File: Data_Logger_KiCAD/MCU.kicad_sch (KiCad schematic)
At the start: 39 parts, among them J1 USB_C_Receptacle_USB2.0_16P, J2 Screw_Terminal_01x02, Q1 Q_NMOS_GSD, SW1 SW_Push, SW2 SW_Push, U2 ESP32-S3, Y2 Crystal, Y3 Crystal_GND24

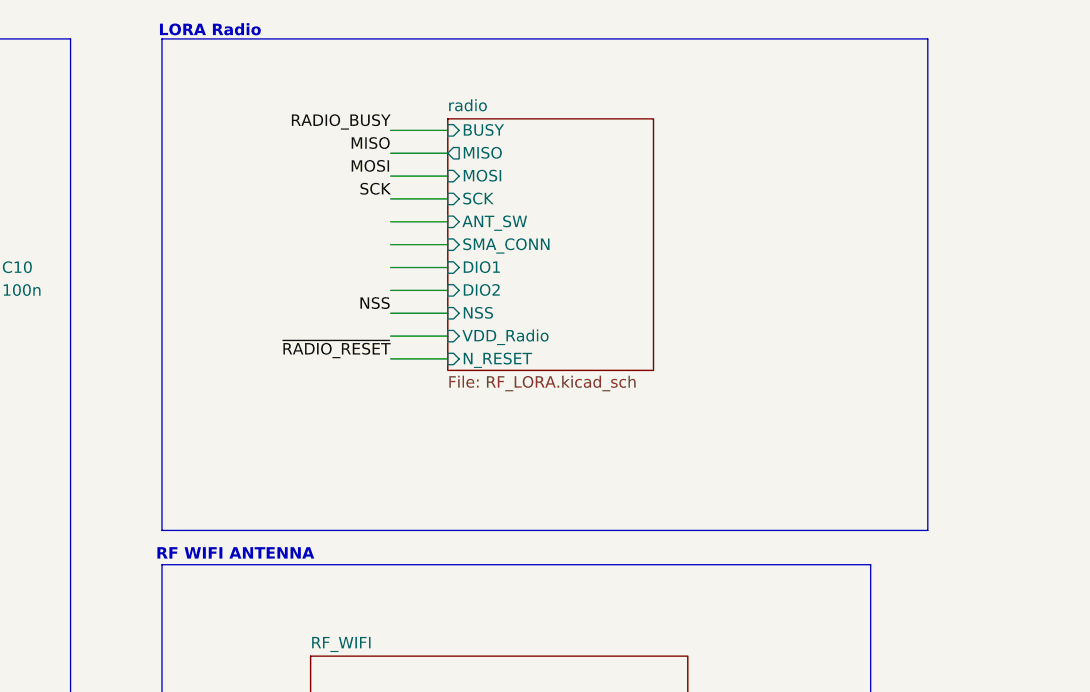
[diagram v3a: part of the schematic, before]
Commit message: update sheet pins
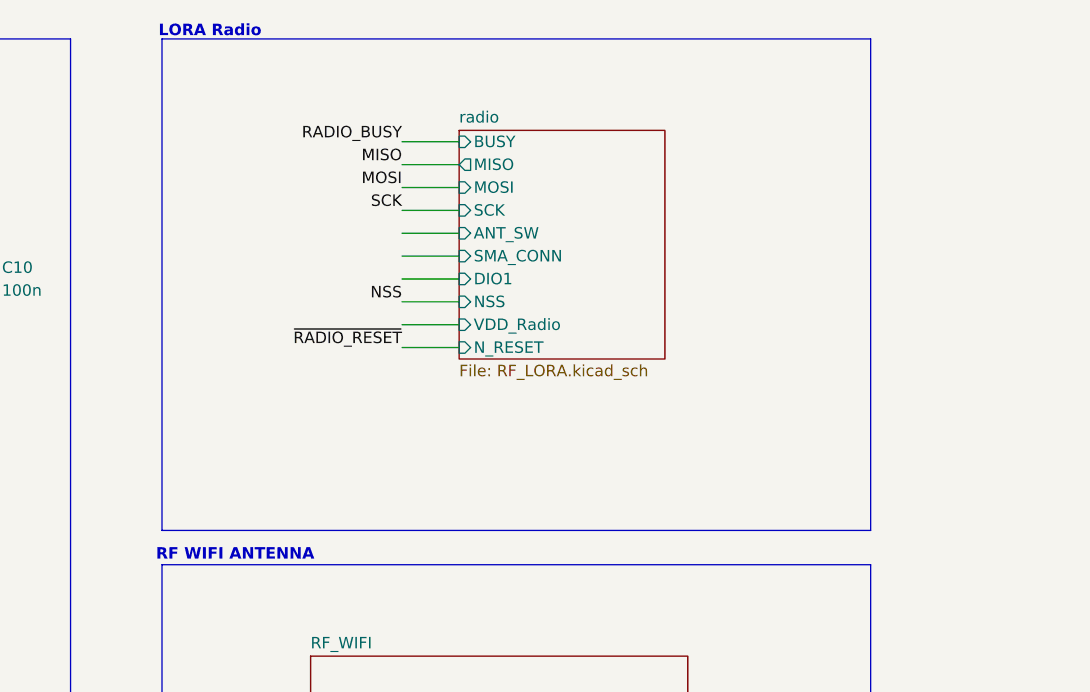
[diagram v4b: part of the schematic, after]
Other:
- sheet radio ports: added none; removed DIO2
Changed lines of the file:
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@@
 	(rectangle
 		(start 242.57 53.34)
-		(end 327.66 107.95)
+		(end 321.31 107.95)
 		(stroke
 			(width 0)
@@
 	(wire
 		(pts
-			(xy 267.97 68.58) (xy 274.32 68.58)
+			(xy 269.24 69.85) (xy 275.59 69.85)
 		)
 		(stroke
@@
 	(wire
 		(pts
+			(xy 269.24 85.09) (xy 275.59 85.09)
+		)
+		(stroke
+			(width 0)
+			(type default)
+		)
+	)
+	(wire
+		(pts
 			(xy 66.04 72.39) (xy 68.58 72.39)
 		)
@@
 	(wire
 		(pts
+			(xy 269.24 87.63) (xy 275.59 87.63)
+		)
+		(stroke
+			(width 0)
+			(type default)
+		)
+	)
+	(wire
+		(pts
 			(xy 132.08 95.25) (xy 139.7 95.25)
 		)
@@
 	(wire
 		(pts
-			(xy 267.97 71.12) (xy 274.32 71.12)
+			(xy 269.24 72.39) (xy 275.59 72.39)
 		)
 		(stroke
@@
 	(wire
 		(pts
-			(xy 33.02 306.07) (xy 40.64 306.07)
+			(xy 269.24 82.55) (xy 275.59 82.55)
 		)
 		(stroke
@@
 	(wire
 		(pts
-			(xy 63.5 306.07) (xy 63.5 307.34)
+			(xy 33.02 306.07) (xy 40.64 306.07)
 		)
 		(stroke
@@
 	(wire
 		(pts
-			(xy 185.42 151.13) (xy 193.04 151.13)
+			(xy 63.5 306.07) (xy 63.5 307.34)
 		)
 		(stroke
@@
 	(wire
 		(pts
-			(xy 53.34 157.48) (xy 53.34 160.02)
+			(xy 185.42 151.13) (xy 193.04 151.13)
 		)
 		(stroke
@@
 	(wire
 		(pts
-			(xy 55.88 85.09) (xy 59.69 85.09)
+			(xy 53.34 157.48) (xy 53.34 160.02)
 		)
 		(stroke
@@
 	(wire
 		(pts
-			(xy 267.97 81.28) (xy 274.32 81.28)
+			(xy 55.88 85.09) (xy 59.69 85.09)
 		)
 		(stroke
@@
 	(wire
 		(pts
-			(xy 267.97 78.74) (xy 274.32 78.74)
+			(xy 269.24 80.01) (xy 275.59 80.01)
 		)
 		(stroke
@@
 	(wire
 		(pts
-			(xy 267.97 73.66) (xy 274.32 73.66)
+			(xy 269.24 74.93) (xy 275.59 74.93)
 		)
 		(stroke
@@
 	(wire
 		(pts
-			(xy 267.97 86.36) (xy 274.32 86.36)
-		)
-		(stroke
-			(width 0)
-			(type default)
-		)
-	)
-	(wire
-		(pts
 			(xy 60.96 62.23) (xy 60.96 67.31)
 		)
@@
 	(wire
 		(pts
-			(xy 267.97 76.2) (xy 274.32 76.2)
+			(xy 269.24 77.47) (xy 275.59 77.47)
 		)
 		(stroke
@@
 	(wire
 		(pts
-			(xy 267.97 83.82) (xy 274.32 83.82)
-		)
-		(stroke
-			(width 0)
-			(type default)
-		)
-	)
-	(wire
-		(pts
 			(xy 185.42 100.33) (xy 207.01 100.33)
 		)
@@
 	(wire
 		(pts
-			(xy 267.97 66.04) (xy 274.32 66.04)
+			(xy 269.24 67.31) (xy 275.59 67.31)
 		)
 		(stroke
@@
 	(wire
 		(pts
-			(xy 267.97 63.5) (xy 274.32 63.5)
+			(xy 269.24 64.77) (xy 275.59 64.77)
 		)
 		(stroke
@@
 	(wire
 		(pts
-			(xy 267.97 88.9) (xy 274.32 88.9)
-		)
-		(stroke
-			(width 0)
-			(type default)
-		)
-	)
-	(wire
-		(pts
 			(xy 300.99 182.88) (xy 307.34 182.88)
 		)
@@
 	)
 	(label "MOSI"
-		(at 267.97 68.58 180)
+		(at 269.24 69.85 180)
 		(effects
 			(font
@@
 	)
 	(label "MISO"
-		(at 267.97 66.04 180)
+		(at 269.24 67.31 180)
 		(effects
 			(font
@@
 	)
 	(label "~{RADIO_RESET}"
-		(at 267.97 88.9 180)
+		(at 269.24 87.63 180)
 		(effects
 			(font
@@
 	)
 	(label "SCK"
-		(at 267.97 71.12 180)
+		(at 269.24 72.39 180)
 		(effects
 			(font
@@
 	)
 	(label "NSS"
-		(at 267.97 83.82 180)
+		(at 269.24 82.55 180)
 		(effects
 			(font
@@
 	)
 	(label "RADIO_BUSY"
-		(at 267.97 63.5 180)
+		(at 269.24 64.77 180)
 		(effects
 			(font
@@
 	)
 	(sheet
-		(at 274.32 62.23)
-		(size 22.86 27.94)
+		(at 275.59 63.5)
+		(size 22.86 25.4)
 		(exclude_from_sim no)
 		(in_bom yes)
@@
 		)
 		(property "Sheetname" "radio"
-			(at 274.32 61.5184 0)
+			(at 275.59 62.7884 0)
 			(effects
 				(font
@@
 		)
 		(property "Sheetfile" "RF_LORA.kicad_sch"
-			(at 274.32 90.7546 0)
+			(at 275.59 89.4846 0)
 			(effects
 				(font
@@
 		)
 		(pin "ANT_SW" input
-			(at 274.32 73.66 180)
+			(at 275.59 74.93 180)
 			(effects
 				(font
@@
 		)
 		(pin "DIO1" input
-			(at 274.32 78.74 180)
-			(effects
-				(font
-					(size 1.27 1.27)
-				)
-				(justify left)
-			)
-		)
-		(pin "DIO2" input
-			(at 274.32 81.28 180)
+			(at 275.59 80.01 180)
 			(effects
 				(font
@@
 		)
 		(pin "MISO" output
-			(at 274.32 66.04 180)
+			(at 275.59 67.31 180)
 			(effects
 				(font
@@
 		)
 		(pin "BUSY" input
-			(at 274.32 63.5 180)
+			(at 275.59 64.77 180)
 			(effects
 				(font
@@
 		)
 		(pin "VDD_Radio" input
-			(at 274.32 86.36 180)
+			(at 275.59 85.09 180)
 			(effects
 				(font
@@
 		)
 		(pin "SMA_CONN" input
-			(at 274.32 76.2 180)
+			(at 275.59 77.47 180)
 			(effects
 				(font
@@
 		)
 		(pin "SCK" input
-			(at 274.32 71.12 180)
+			(at 275.59 72.39 180)
 			(effects
 				(font
@@
 		)
 		(pin "MOSI" input
-			(at 274.32 68.58 180)
+			(at 275.59 69.85 180)
 			(effects
 				(font
@@
 		)
 		(pin "NSS" input
-			(at 274.32 83.82 180)
+			(at 275.59 82.55 180)
 			(effects
 				(font
@@
 		)
 		(pin "N_RESET" input
-			(at 274.32 88.9 180)
+			(at 275.59 87.63 180)
 			(effects
 				(font

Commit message: add more footprints
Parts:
- R13, R14, R3, R4, R5, R6, R7: footprint (none) -> Resistor_SMD:R_0402_1005Metric
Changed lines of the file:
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@@
 			)
 		)
-		(property "Footprint" ""
+		(property "Footprint" "Resistor_SMD:R_0402_1005Metric"
 			(at 207.772 135.89 90)
 			(effects
@@
 			)
 		)
-		(property "Footprint" ""
+		(property "Footprint" "Resistor_SMD:R_0402_1005Metric"
 			(at 60.452 199.39 90)
 			(effects
@@
 			)
 		)
-		(property "Footprint" ""
+		(property "Footprint" "Resistor_SMD:R_0402_1005Metric"
 			(at 51.562 143.51 90)
 			(effects
@@
 			)
 		)
-		(property "Footprint" ""
+		(property "Footprint" "Resistor_SMD:R_0402_1005Metric"
 			(at 41.91 365.76 0)
 			(effects
@@
 			)
 		)
-		(property "Footprint" ""
+		(property "Footprint" "Resistor_SMD:R_0402_1005Metric"
 			(at 44.45 361.95 0)
 			(effects
@@
 			)
 		)
-		(property "Footprint" ""
+		(property "Footprint" "Resistor_SMD:R_0402_1005Metric"
 			(at 51.562 153.67 90)
 			(effects
@@
 			)
 		)
-		(property "Footprint" ""
+		(property "Footprint" "Resistor_SMD:R_0402_1005Metric"
 			(at 215.392 135.89 90)
 			(effects

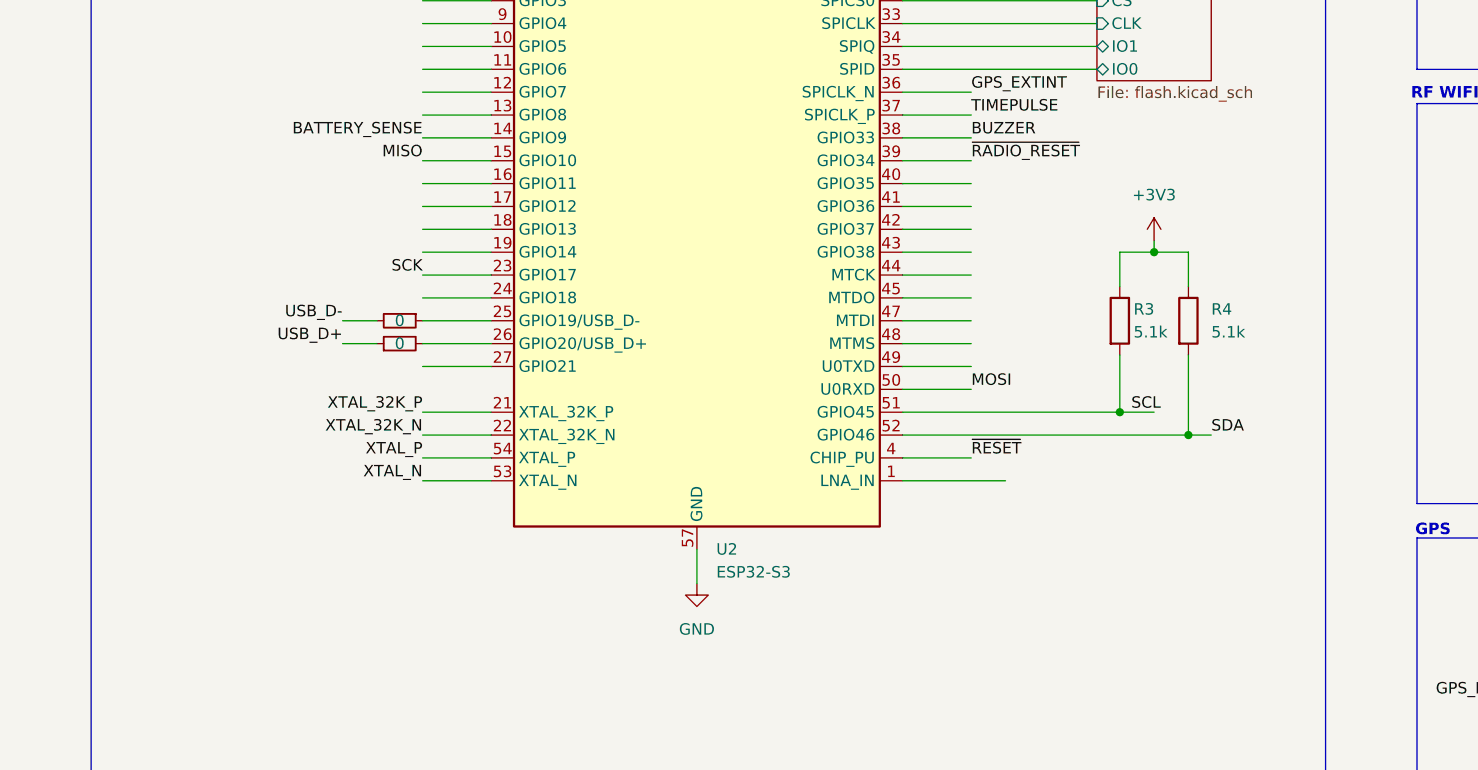
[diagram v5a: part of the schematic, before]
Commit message: adding labels and updating IMU sch
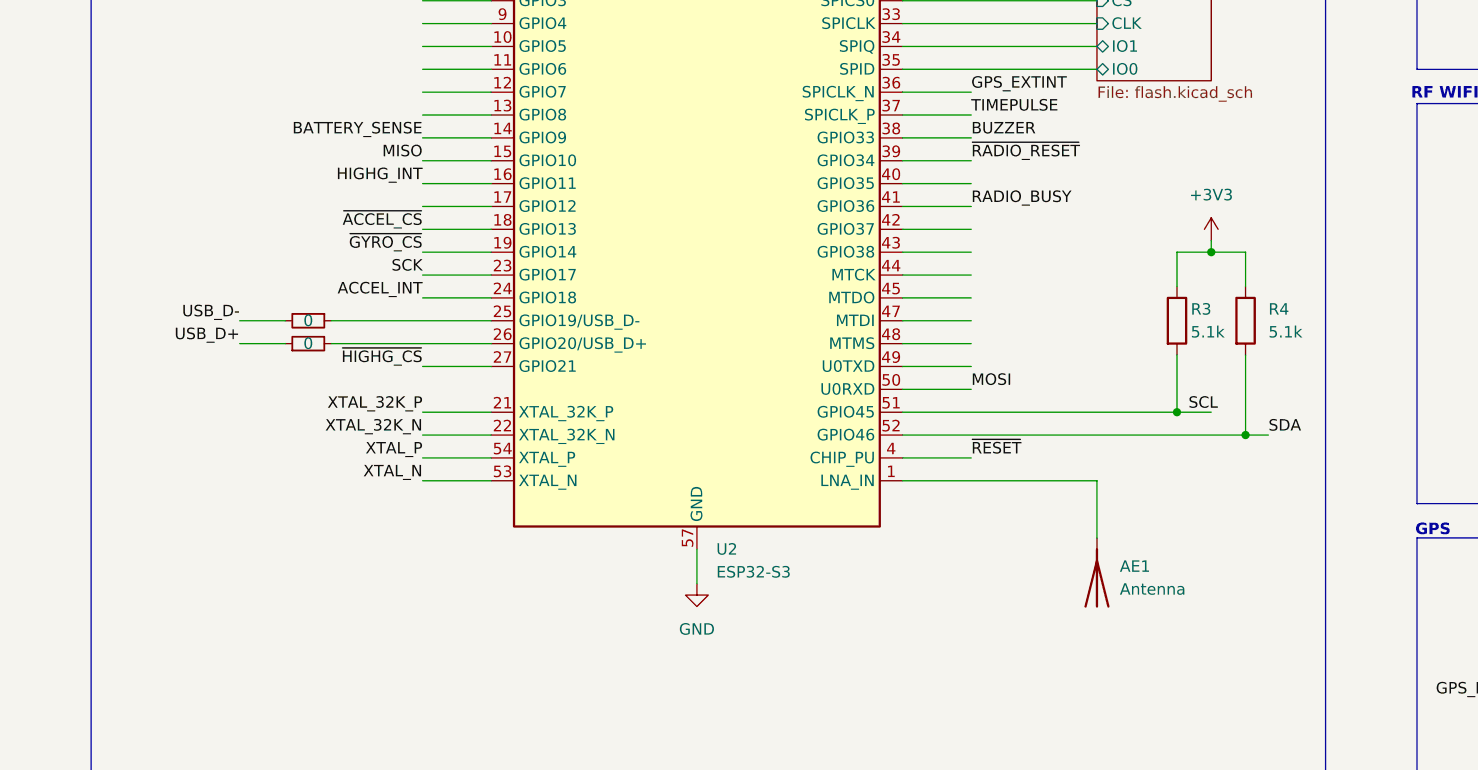
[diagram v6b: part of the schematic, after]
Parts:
- added AE1: Antenna, symbol Device:Antenna
- R11, R12: footprint (none) -> Resistor_SMD:R_0402_1005Metric
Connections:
- net RADIO_BUSY: now also U2.41 (GPIO36)
- net at U2.1 (LNA_IN): now also AE1.1 (A)
- net HIGHG_INT: now reaches U2.16 (GPIO11)
- net ~{ACCEL_CS}: now reaches U2.18 (GPIO13)
- net ~{GYRO_CS}: now reaches U2.19 (GPIO14)
- net ACCEL_INT: now reaches U2.24 (GPIO18)
- net ~{HIGHG_CS}: now reaches U2.27 (GPIO21)
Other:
- moved on the sheet: R3, R4

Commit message: update MCU
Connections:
- net MS_CS: now reaches U2.6 (GPIO1)
- net BMP_CS: now reaches U2.7 (GPIO2)
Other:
- sheet IMU ports: added ACCEL_INT, CS_IMU, HIGHG_INT, MISO, MOSI, SCK, SDI, SDO, SPC, ~{ACCEL_CS}, ~{GYRO_CS}, ~{HIGHG_CS}; removed none

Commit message: add CS's
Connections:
- net MAG_CS: now also U2.8 (GPIO3)
- net MAG_INT: now also U2.10 (GPIO5)
- net IMU_CS: now reaches U2.9 (GPIO4)
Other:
- sheet IMU ports: added IMU_CS; removed CS_IMU, SDI, SDO, SPC
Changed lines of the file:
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@@
 	(wire
 		(pts
+			(xy 147.32 232.41) (xy 153.67 232.41)
+		)
+		(stroke
+			(width 0)
+			(type default)
+		)
+	)
+	(wire
+		(pts
 			(xy 53.34 148.59) (xy 53.34 149.86)
 		)
@@
 	(wire
 		(pts
+			(xy 153.67 245.11) (xy 147.32 245.11)
+		)
+		(stroke
+			(width 0)
+			(type default)
+		)
+	)
+	(wire
+		(pts
 			(xy 53.34 147.32) (xy 53.34 148.59)
 		)
@@
 	(wire
 		(pts
+			(xy 147.32 237.49) (xy 153.67 237.49)
+		)
+		(stroke
+			(width 0)
+			(type default)
+		)
+	)
+	(wire
+		(pts
 			(xy 165.1 85.09) (xy 165.1 74.93)
 		)
@@
 	(wire
 		(pts
+			(xy 147.32 224.79) (xy 153.67 224.79)
+		)
+		(stroke
+			(width 0)
+			(type default)
+		)
+	)
+	(wire
+		(pts
 			(xy 50.8 189.23) (xy 60.96 189.23)
 		)
@@
 	(wire
 		(pts
+			(xy 147.32 227.33) (xy 153.67 227.33)
+		)
+		(stroke
+			(width 0)
+			(type default)
+		)
+	)
+	(wire
+		(pts
 			(xy 255.27 182.88) (xy 262.89 182.88)
 		)
@@
 	(wire
 		(pts
+			(xy 147.32 240.03) (xy 153.67 240.03)
+		)
+		(stroke
+			(width 0)
+			(type default)
+		)
+	)
+	(wire
+		(pts
 			(xy 185.42 143.51) (xy 193.04 143.51)
 		)
@@
 	(wire
 		(pts
+			(xy 147.32 242.57) (xy 153.67 242.57)
+		)
+		(stroke
+			(width 0)
+			(type default)
+		)
+	)
+	(wire
+		(pts
 			(xy 38.1 361.95) (xy 41.91 361.95)
 		)
@@
 	(wire
 		(pts
+			(xy 147.32 234.95) (xy 153.67 234.95)
+		)
+		(stroke
+			(width 0)
+			(type default)
+		)
+	)
+	(wire
+		(pts
 			(xy 157.48 74.93) (xy 148.59 74.93)
 		)
@@
 		)
 	)
+	(wire
+		(pts
+			(xy 147.32 229.87) (xy 153.67 229.87)
+		)
+		(stroke
+			(width 0)
+			(type default)
+		)
+	)
 	(label "USB_D-"
 		(at 111.76 135.89 180)
@@
 		)
 	)
+	(label "HIGHG_INT"
+		(at 147.32 245.11 180)
+		(effects
+			(font
+				(size 1.27 1.27)
+			)
+			(justify right bottom)
+		)
+	)
+	(label "MISO"
+		(at 147.32 242.57 180)
+		(effects
+			(font
+				(size 1.27 1.27)
+			)
+			(justify right bottom)
+		)
+	)
 	(label "SCK"
 		(at 445.77 69.85 0)
@@
 		)
 	)
+	(label "IMU_CS"
+		(at 132.08 102.87 180)
+		(effects
+			(font
+				(size 1.27 1.27)
+			)
+			(justify right bottom)
+		)
+	)
+	(label "SCK"
+		(at 147.32 229.87 180)
+		(effects
+			(font
+				(size 1.27 1.27)
+			)
+			(justify right bottom)
+		)
+	)
+	(label "MAG_INT"
+		(at 132.08 105.41 180)
+		(effects
+			(font
+				(size 1.27 1.27)
+			)
+			(justify right bottom)
+		)
+	)
 	(label "BUZZER"
 		(at 38.1 361.95 180)
@@
 		)
 	)
+	(label "ACCEL_INT"
+		(at 147.32 240.03 180)
+		(effects
+			(font
+				(size 1.27 1.27)
+			)
+			(justify right bottom)
+		)
+	)
 	(label "XTAL_P"
 		(at 132.08 151.13 180)
@@
 		)
 	)
+	(label "~{ACCEL_CS}"
+		(at 147.32 232.41 180)
+		(effects
+			(font
+				(size 1.27 1.27)
+			)
+			(justify right bottom)
+		)
+	)
 	(label "SDA"
 		(at 226.06 148.59 0)
@@
 		)
 	)
+	(label "IMU_CS"
+		(at 147.32 224.79 180)
+		(effects
+			(font
+				(size 1.27 1.27)
+			)
+			(justify right bottom)
+		)
+	)
 	(label "BOOT"
 		(at 60.96 189.23 0)
@@
 		)
 	)
+	(label "MAG_CS"
+		(at 132.08 100.33 180)
+		(effects
+			(font
+				(size 1.27 1.27)
+			)
+			(justify right bottom)
+		)
+	)
 	(label "XTAL_P"
 		(at 68.58 297.18 0)
@@
 		)
 	)
+	(label "MOSI"
+		(at 147.32 227.33 180)
+		(effects
+			(font
+				(size 1.27 1.27)
+			)
+			(justify right bottom)
+		)
+	)
+	(label "~{GYRO_CS}"
+		(at 147.32 234.95 180)
+		(effects
+			(font
+				(size 1.27 1.27)
+			)
+			(justify right bottom)
+		)
+	)
 	(label "XTAL_N"
 		(at 132.08 153.67 180)
@@
 		)
 	)
+	(label "~{HIGHG_CS}"
+		(at 147.32 237.49 180)
+		(effects
+			(font
+				(size 1.27 1.27)
+			)
+			(justify right bottom)
+		)
+	)
 	(label "BATTERY_SENSE"
 		(at 132.08 115.57 180)
@@
 	)
 	(sheet
-		(at 143.51 219.71)
-		(size 38.1 33.02)
+		(at 153.67 222.25)
+		(size 27.94 25.4)
 		(exclude_from_sim no)
 		(in_bom yes)
@@
 		)
 		(property "Sheetname" "IMU"
-			(at 143.51 218.9984 0)
+			(at 153.67 221.5384 0)
 			(effects
 				(font
@@
 		)
 		(property "Sheetfile" "IMU.kicad_sch"
-			(at 143.51 253.3146 0)
+			(at 153.67 248.2346 0)
 			(effects
 				(font
@@
 		)
 		(pin "ACCEL_INT" output
-			(at 143.51 242.57 180)
-			(effects
-				(font
-					(size 1.27 1.27)
-				)
-				(justify left)
-			)
-		)
-		(pin "CS_IMU" input
-			(at 143.51 222.25 180)
+			(at 153.67 240.03 180)
 			(effects
 				(font
@@
 		)
 		(pin "HIGHG_INT" output
-			(at 143.51 250.19 180)
+			(at 153.67 245.11 180)
 			(effects
 				(font
@@
 		)
 		(pin "MISO" output
-			(at 143.51 247.65 180)
+			(at 153.67 242.57 180)
 			(effects
 				(font
@@
 		)
 		(pin "MOSI" input
-			(at 143.51 224.79 180)
+			(at 153.67 227.33 180)
 			(effects
 				(font
@@
 		)
 		(pin "SCK" input
-			(at 143.51 227.33 180)
-			(effects
-				(font
-					(size 1.27 1.27)
-				)
-				(justify left)
-			)
-		)
-		(pin "SDI" input
-			(at 143.51 229.87 180)
-			(effects
-				(font
-					(size 1.27 1.27)
-				)
-				(justify left)
-			)
-		)
-		(pin "SDO" output
-			(at 143.51 245.11 180)
+			(at 153.67 229.87 180)
 			(effects
 				(font
@@
 			)
 		)
-		(pin "SPC" input
-			(at 143.51 232.41 180)
+		(pin "~{ACCEL_CS}" input
+			(at 153.67 232.41 180)
 			(effects
 				(font
@@
 			)
 		)
-		(pin "~{ACCEL_CS}" input
-			(at 143.51 234.95 180)
+		(pin "~{GYRO_CS}" input
+			(at 153.67 234.95 180)
 			(effects
 				(font
@@
 			)
 		)
-		(pin "~{GYRO_CS}" input
-			(at 143.51 237.49 180)
+		(pin "~{HIGHG_CS}" input
+			(at 153.67 237.49 180)
 			(effects
 				(font
@@
 			)
 		)
-		(pin "~{HIGHG_CS}" input
-			(at 143.51 240.03 180)
+		(pin "IMU_CS" input
+			(at 153.67 224.79 180)
 			(effects
 				(font
